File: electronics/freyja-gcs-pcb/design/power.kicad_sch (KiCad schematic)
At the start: 113 parts, among them J6 GT-USB-7010ASV, J7 A2543WR-4P-2, J8 XD-PH-10AW, J9 JS350-S02DCA-00, Q1 TM10N06SI, Q2 TM10N06SI, Q3 AO4459, Q4 L2N7002SLLT1G, Q5 L2N7002SLLT1G, Q6 TM10N06SI, Q7 TM10N06SI, Q8 TM10N06SI, SW3 K6-6136D-L1-04, U10 LM74700QDBVRQ1, U11 AMS1117-3.3, U12 RY3730, U3 FM7021DB, U4 CN3702, U5 HY2213-BB3A, U6 HY2213-BB3A, U7 IP2721, U8 SY8368AQQC, U9 LM74700QDBVRQ1

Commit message: power layout wip
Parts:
- C29: value 100n -> 22u; footprint Capacitor_SMD:C_0603_1608Metric -> EasyEDA:C1210; LCSC Part C2762593 -> C100086
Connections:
- net +5V: now also C29.1
- net VPWR: no longer C29.1
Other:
- moved on the sheet: C27, C28, C42, C44, D30, J9, L3, R37, TP7, U12

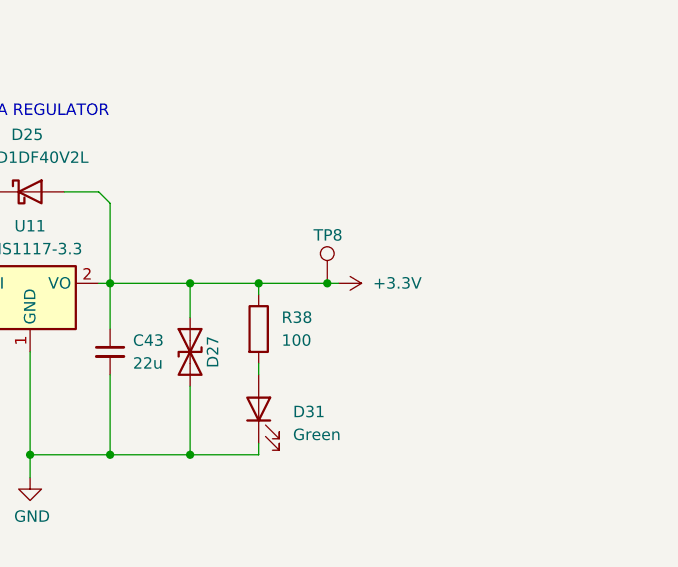
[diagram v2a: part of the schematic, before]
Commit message: locked position of components
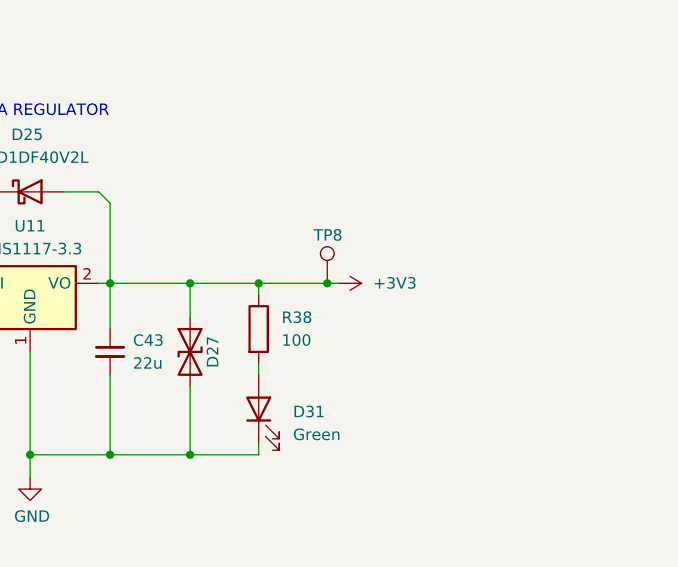
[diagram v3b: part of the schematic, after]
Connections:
- net +3.3V renamed +3V3
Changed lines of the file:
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@@
+	)
+	(symbol
+		(lib_id "power:+3V3")
+		(at 369.57 163.83 270)
+		(unit 1)
+		(exclude_from_sim no)
+		(in_bom yes)
+		(on_board yes)
+		(dnp no)
+		(fields_autoplaced yes)
+		(property "Reference" "#PWR0121"
+			(at 365.76 163.83 0)
+			(effects
+				(font
+					(size 1.27 1.27)
+				)
+				(hide yes)
+			)
+		)
+		(property "Value" "+3V3"
+			(at 373.38 163.8299 90)
+			(effects
+				(font
+					(size 1.27 1.27)
+				)
+				(justify left)
+			)
+		)
+		(property "Footprint" ""
+			(at 369.57 163.83 0)
+			(effects
+				(font
+					(size 1.27 1.27)
+				)
+				(hide yes)
+			)
+		)
+		(property "Datasheet" ""
+			(at 369.57 163.83 0)
+			(effects
+				(font
+					(size 1.27 1.27)
+				)
+				(hide yes)
+			)
+		)
+		(property "Description" "Power symbol creates a global label with name \"+3V3\""
+			(at 369.57 163.83 0)
+			(effects
+				(font
+					(size 1.27 1.27)
+				)
+				(hide yes)
+			)
+		)
+		(pin "1"
+		)
+		(instances
+			(project ""
+				(path "/c292fa04-82ad-49e9-a9d8-422554d1d11d/c65c6484-459d-48da-abd0-c2a58ebde1bb"
+					(reference "#PWR0121")
+					(unit 1)
+				)
+			)
+		)
 	)
 	(symbol
@@
 					(unit 1)
 				)
-			)
-		)
-	)
-	(symbol
-		(lib_id "power:+3.3V")
-		(at 369.57 163.83 270)
-		(unit 1)
-		(exclude_from_sim no)
-		(in_bom yes)
-		(on_board yes)
-		(dnp no)
-		(fields_autoplaced yes)
-		(property "Reference" "#PWR063"
-			(at 365.76 163.83 0)
-			(effects
-				(font
-					(size 1.27 1.27)
-				)
-				(hide yes)
-			)
-		)
-		(property "Value" "+3.3V"
-			(at 373.38 163.8299 90)
-			(effects
-				(font
-					(size 1.27 1.27)
-				)
-				(justify left)
-			)
-		)
-		(property "Footprint" ""
-			(at 369.57 163.83 0)
-			(effects
-				(font
-					(size 1.27 1.27)
-				)
-				(hide yes)
-			)
-		)
-		(property "Datasheet" ""
-			(at 369.57 163.83 0)
-			(effects
-				(font
-					(size 1.27 1.27)
-				)
-				(hide yes)
-			)
-		)
-		(property "Description" "Power symbol creates a global label with name \"+3.3V\""
-			(at 369.57 163.83 0)
-			(effects
-				(font
-					(size 1.27 1.27)
-				)
-				(hide yes)
-			)
-		)
-		(pin "1"
-		)
-		(instances
-			(project ""
-				(path "/c292fa04-82ad-49e9-a9d8-422554d1d11d/c65c6484-459d-48da-abd0-c2a58ebde1bb"
-					(reference "#PWR063")
-					(unit 1)
-				)

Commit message: mcu layout
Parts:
- added D59: PSBD1DF40V2L, EasyEDA:SOD-123FL_L2.8-W1.8-LS3.8-RD, symbol Device:D_Schottky
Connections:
- net +5V: now also D59.1 (K)
- net VBAT: now also U10.3 (EN)
- net VBUS: now also U9.3 (EN)
- net at C34.1, U9.1 (VCAP): no longer U9.3 (EN)
- net at C35.1, U10.1 (VCAP): no longer U10.3 (EN)
- new net VBUS_DEV: D59.2 (A)
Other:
- moved on the sheet: C30, C31, C32, C33, C34, C35, TP6

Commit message: usb pd layout
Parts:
- added D60: PESD2IVN24-TR, EasyEDA:TO-236AB_L2.9-W1.3-P0.95-LS2.3-BR, symbol EasyEDA:PESD2IVN24-TR
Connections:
- net GND: now also D60.3
- net at C23.1, J6.A4B9 (VBUS), J6.B4A9 (VBUS)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: now also D60.1, D60.2
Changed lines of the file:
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@@
 	)
 	(junction
+		(at 138.43 44.45)
+		(diameter 0)
+		(color 0 0 0 0)
+	)
+	(junction
 		(at 322.58 218.44)
 		(diameter 0)
@@
 	)
 	(junction
+		(at 148.59 44.45)
+		(diameter 0)
+		(color 0 0 0 0)
+	)
+	(junction
 		(at 262.89 207.01)
 		(diameter 0)
@@
 	(wire
 		(pts
+			(xy 148.59 44.45) (xy 148.59 49.53)
+		)
+		(stroke
+			(width 0)
+			(type default)
+		)
+	)
+	(wire
+		(pts
 			(xy 168.91 76.2) (xy 170.18 77.47)
 		)
@@
 	(wire
 		(pts
-			(xy 93.98 44.45) (xy 137.16 44.45)
+			(xy 93.98 44.45) (xy 138.43 44.45)
 		)
 		(stroke
@@
 	(wire
 		(pts
-			(xy 138.43 45.72) (xy 138.43 63.5)
+			(xy 138.43 44.45) (xy 138.43 63.5)
 		)
 		(stroke
@@
 	(wire
 		(pts
+			(xy 173.99 46.99) (xy 175.26 46.99)
+		)
+		(stroke
+			(width 0)
+			(type default)
+		)
+	)
+	(wire
+		(pts
 			(xy 39.37 176.53) (xy 48.26 176.53)
 		)
@@
 	(wire
 		(pts
-			(xy 137.16 44.45) (xy 138.43 45.72)
-		)
-		(stroke
-			(width 0)
-			(type default)
-		)
-	)
-	(wire
-		(pts
 			(xy 85.09 167.64) (xy 85.09 168.91)
 		)
@@
 	(wire
 		(pts
+			(xy 175.26 46.99) (xy 175.26 48.26)
+		)
+		(stroke
+			(width 0)
+			(type default)
+		)
+	)
+	(wire
+		(pts
 			(xy 96.52 154.94) (xy 96.52 168.91)
 		)
@@
 	(wire
 		(pts
+			(xy 138.43 44.45) (xy 148.59 44.45)
+		)
+		(stroke
+			(width 0)
+			(type default)
+		)
+	)
+	(wire
+		(pts
 			(xy 246.38 101.6) (xy 246.38 104.14)
 		)
@@
 	)
 	(symbol
+		(lib_id "EasyEDA:PESD2IVN24-TR")
+		(at 161.29 46.99 0)
+		(mirror x)
+		(unit 1)
+		(exclude_from_sim no)
+		(in_bom yes)
+		(on_board yes)
+		(dnp no)
+		(property "Reference" "D60"
+			(at 160.0199 53.34 90)
+			(effects
+				(font
+					(size 1.27 1.27)
+				)
+				(justify left)
+			)
+		)
+		(property "Value" "PESD2IVN24-TR"
+			(at 162.5599 53.34 90)
+			(effects
+				(font
+					(size 1.27 1.27)
+				)
+				(justify left)
+			)
+		)
+		(property "Footprint" "EasyEDA:TO-236AB_L2.9-W1.3-P0.95-LS2.3-BR"
+			(at 161.29 36.83 0)
+			(effects
+				(font
+					(size 1.27 1.27)
+				)
+				(hide yes)
+			)
+		)
+		(property "Datasheet" "https://lcsc.com/product-detail/Zener-Diodes_Nexperia-PESD2IVN24-TR_C406047.html"
+			(at 161.29 34.29 0)
+			(effects
+				(font
+					(size 1.27 1.27)
+				)
+				(hide yes)
+			)
+		)
+		(property "Description" ""
+			(at 161.29 46.99 0)
+			(effects
+				(font
+					(size 1.27 1.27)
+				)
+				(hide yes)
+			)
+		)
+		(property "LCSC Part" "C406047"
+			(at 161.29 31.75 0)
+			(effects
+				(font
+					(size 1.27 1.27)
+				)
+				(hide yes)
+			)
+		)
+		(pin "2"
+		)
+		(pin "3"
+		)
+		(pin "1"
+		)
+		(instances
+			(project "freyja-gcs-pcb"
+				(path "/c292fa04-82ad-49e9-a9d8-422554d1d11d/c65c6484-459d-48da-abd0-c2a58ebde1bb"
+					(reference "D60")
+					(unit 1)
+				)
+			)
+		)
+	)
+	(symbol
 		(lib_id "Device:R")
 		(at 274.32 201.93 270)
@@
 					(unit 1)
 				)
+			)
+		)
+	)
+	(symbol
+		(lib_id "power:GND")
+		(at 175.26 48.26 0)
+		(mirror y)
+		(unit 1)
+		(exclude_from_sim no)
+		(in_bom yes)
+		(on_board yes)
+		(dnp no)
+		(property "Reference" "#PWR05"
+			(at 175.26 54.61 0)
+			(effects
+				(font
+					(size 1.27 1.27)
+				)
+				(hide yes)
+			)
+		)
+		(property "Value" "GND"
+			(at 173.482 52.578 0)
+			(effects
+				(font
+					(size 1.27 1.27)
+				)
+				(justify right)
+			)
+		)
+		(property "Footprint" ""
+			(at 175.26 48.26 0)
+			(effects
+				(font
+					(size 1.27 1.27)
+				)
+				(hide yes)
+			)
+		)
+		(property "Datasheet" ""
+			(at 175.26 48.26 0)
+			(effects
+				(font
+					(size 1.27 1.27)
+				)
+				(hide yes)
+			)
+		)
+		(property "Description" "Power symbol creates a global label with name \"GND\" , ground"
+			(at 175.26 48.26 0)
+			(effects
+				(font
+					(size 1.27 1.27)
+				)
+				(hide yes)
+			)
+		)
+		(pin "1"
+		)
+		(instances
+			(project "freyja-gcs-pcb"
+				(path "/c292fa04-82ad-49e9-a9d8-422554d1d11d/c65c6484-459d-48da-abd0-c2a58ebde1bb"
+					(reference "#PWR05")
+					(unit 1)
+				)

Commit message: charging circuit layout wip
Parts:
- added C49: 22u, EasyEDA:C2220, symbol Device:C_Small
- added TP10: TestPoint, TestPoint:TestPoint_Pad_D3.0mm, symbol Connector:TestPoint
- C20: value 100n -> 470n; LCSC Part C2762593 -> C513577
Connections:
- net BAT-: no longer R11.2
- net GND: now also C49.2
- net VBAT: now also C49.1
- net at BT4.1 (-), BT5.2 (+), C21.2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: now also BT2.1 (-), BT3.2 (+), TP10.1
- net at U3.3 (CS): now also R11.2
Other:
- moved on the sheet: Q1, Q2, R11

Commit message: btn routing wip
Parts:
- D13: footprint EasyEDA:LED0603-RD_GREEN -> EasyEDA:LED-TH_BD5.9-P2.54-RD_GREEN; LCSC Part C965804 -> C2895548
- D14: value Amber -> Yellow; footprint EasyEDA:LED0603-R-RD_AMBER -> EasyEDA:LED-TH_BD5.9-P2.54-RD_GREEN; LCSC Part C510024 -> C2895494
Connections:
- net at U4.4 (~{CHRG}): now also D14.1 (K); no longer D14.2 (K)
- net at R15.2: now also D14.2 (A); no longer D14.1 (A)
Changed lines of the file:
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@@
 	)
 	(symbol
-		(lib_name "LED_1")
-		(lib_id "Device:LED")
-		(at 35.56 143.51 90)
-		(unit 1)
-		(exclude_from_sim no)
-		(in_bom yes)
-		(on_board yes)
-		(dnp no)
-		(fields_autoplaced yes)
-		(property "Reference" "D14"
-			(at 39.37 143.8274 90)
-			(effects
-				(font
-					(size 1.27 1.27)
-				)
-				(justify right)
-			)
-		)
-		(property "Value" "Amber"
-			(at 39.37 146.3674 90)
-			(effects
-				(font
-					(size 1.27 1.27)
-				)
-				(justify right)
-			)
-		)
-		(property "Footprint" "EasyEDA:LED0603-R-RD_AMBER"
-			(at 35.56 143.51 0)
-			(effects
-				(font
-					(size 1.27 1.27)
-				)
-				(hide yes)
-			)
-		)
-		(property "Datasheet" "~"
-			(at 35.56 143.51 0)
-			(effects
-				(font
-					(size 1.27 1.27)
-				)
-				(hide yes)
-			)
-		)
-		(property "Description" "SML-D12D8WT86 Light emitting diode"
-			(at 35.56 143.51 0)
-			(effects
-				(font
-					(size 1.27 1.27)
-				)
-				(hide yes)
-			)
-		)
-		(property "LCSC Part" "C510024"
-			(at 45.72 143.51 0)
-			(effects
-				(font
-					(size 1.27 1.27)
-				)
-				(hide yes)
-			)
-		)
-		(property "Sim.Pins" "1=A 2=K"
-			(at 35.56 143.51 0)
-			(effects
-				(font
-					(size 1.27 1.27)
-				)
-				(hide yes)
-			)
-		)
-		(pin "2"
-		)
-		(pin "1"
-		)
-		(instances
-			(project "freyja-gcs-pcb"
-				(path "/c292fa04-82ad-49e9-a9d8-422554d1d11d/c65c6484-459d-48da-abd0-c2a58ebde1bb"
-					(reference "D14")
-					(unit 1)
-				)
-			)
-		)
-	)
-	(symbol
 		(lib_id "EasyEDA:AO4459")
 		(at 92.71 132.08 270)
@@
 	)
 	(symbol
+		(lib_id "Device:LED")
+		(at 30.48 143.51 270)
+		(mirror x)
+		(unit 1)
+		(exclude_from_sim no)
+		(in_bom yes)
+		(on_board yes)
+		(dnp no)
+		(property "Reference" "D13"
+			(at 26.67 143.8274 90)
+			(effects
+				(font
+					(size 1.27 1.27)
+				)
+				(justify right)
+			)
+		)
+		(property "Value" "Green"
+			(at 26.67 146.3674 90)
+			(effects
+				(font
+					(size 1.27 1.27)
+				)
+				(justify right)
+			)
+		)
+		(property "Footprint" "EasyEDA:LED-TH_BD5.9-P2.54-RD_GREEN"
+			(at 30.48 143.51 0)
+			(effects
+				(font
+					(size 1.27 1.27)
+				)
+				(hide yes)
+			)
+		)
+		(property "Datasheet" "~"
+			(at 30.48 143.51 0)
+			(effects
+				(font
+					(size 1.27 1.27)
+				)
+				(hide yes)
+			)
+		)
+		(property "Description" "XL-502UGD Light emitting diode"
+			(at 30.48 143.51 0)
+			(effects
+				(font
+					(size 1.27 1.27)
+				)
+				(hide yes)
+			)
+		)
+		(property "LCSC Part" "C2895548"
+			(at 20.32 143.51 0)
+			(effects
+				(font
+					(size 1.27 1.27)
+				)
+				(hide yes)
+			)
+		)
+		(property "Sim.Pins" "1=K 2=A"
+			(at 30.48 143.51 0)
+			(effects
+				(font
+					(size 1.27 1.27)
+				)
+				(hide yes)
+			)
+		)
+		(pin "2"
+		)
+		(pin "1"
+		)
+		(instances
+			(project "freyja-gcs-pcb"
+				(path "/c292fa04-82ad-49e9-a9d8-422554d1d11d/c65c6484-459d-48da-abd0-c2a58ebde1bb"
+					(reference "D13")
+					(unit 1)
+				)
+			)
+		)
+	)
+	(symbol
 		(lib_id "power:GND")
 		(at 346.71 125.73 0)
@@
 	)
 	(symbol
+		(lib_id "Device:LED")
+		(at 35.56 143.51 90)
+		(unit 1)
+		(exclude_from_sim no)
+		(in_bom yes)
+		(on_board yes)
+		(dnp no)
+		(property "Reference" "D14"
+			(at 39.37 143.8274 90)
+			(effects
+				(font
+					(size 1.27 1.27)
+				)
+				(justify right)
+			)
+		)
+		(property "Value" "Yellow"
+			(at 39.37 146.3674 90)
+			(effects
+				(font
+					(size 1.27 1.27)
+				)
+				(justify right)
+			)
+		)
+		(property "Footprint" "EasyEDA:LED-TH_BD5.9-P2.54-RD_GREEN"
+			(at 35.56 143.51 0)
+			(effects
+				(font
+					(size 1.27 1.27)
+				)
+				(hide yes)
+			)
+		)
+		(property "Datasheet" "~"
+			(at 35.56 143.51 0)
+			(effects
+				(font
+					(size 1.27 1.27)
+				)
+				(hide yes)
+			)
+		)
+		(property "Description" "XL-502UYD Light emitting diode"
+			(at 35.56 143.51 0)
+			(effects
+				(font
+					(size 1.27 1.27)
+				)
+				(hide yes)
+			)
+		)
+		(property "LCSC Part" "C2895494"
+			(at 45.72 143.51 0)
+			(effects
+				(font
+					(size 1.27 1.27)
+				)
+				(hide yes)
+			)
+		)
+		(property "Sim.Pins" "1=K 2=A"
+			(at 35.56 143.51 0)
+			(effects
+				(font
+					(size 1.27 1.27)
+				)
+				(hide yes)
+			)
+		)
+		(pin "2"
+		)
+		(pin "1"
+		)
+		(instances
+			(project "freyja-gcs-pcb"
+				(path "/c292fa04-82ad-49e9-a9d8-422554d1d11d/c65c6484-459d-48da-abd0-c2a58ebde1bb"
+					(reference "D14")
+					(unit 1)
+				)
+			)
+		)
+	)
+	(symbol
 		(lib_id "Connector:TestPoint")
 		(at 173.99 246.38 270)
@@
 					(unit 1)
 				)
-			)
-		)
-	)
-	(symbol
-		(lib_id "Device:LED")
-		(at 30.48 143.51 270)
-		(mirror x)
-		(unit 1)
-		(exclude_from_sim no)
-		(in_bom yes)
-		(on_board yes)
-		(dnp no)
-		(property "Reference" "D13"
-			(at 26.67 143.8274 90)
-			(effects
-				(font
-					(size 1.27 1.27)
-				)
-				(justify right)
-			)
-		)
-		(property "Value" "Green"
-			(at 26.67 146.3674 90)
-			(effects
-				(font
-					(size 1.27 1.27)
-				)
-				(justify right)
-			)
-		)
-		(property "Footprint" "EasyEDA:LED0603-RD_GREEN"
-			(at 30.48 143.51 0)
-			(effects
-				(font
-					(size 1.27 1.27)
-				)
-				(hide yes)
-			)
-		)
-		(property "Datasheet" "~"
-			(at 30.48 143.51 0)
-			(effects
-				(font
-					(size 1.27 1.27)
-				)
-				(hide yes)
-			)
-		)
-		(property "Description" "XL-1608UGC-04 Light emitting diode"
-			(at 30.48 143.51 0)
-			(effects
-				(font
-					(size 1.27 1.27)
-				)
-				(hide yes)
-			)
-		)
-		(property "LCSC Part" "C965804"
-			(at 20.32 143.51 0)
-			(effects
-				(font
-					(size 1.27 1.27)
-				)
-				(hide yes)
-			)
-		)
-		(property "Sim.Pins" "1=K 2=A"
-			(at 30.48 143.51 0)
-			(effects
-				(font
-					(size 1.27 1.27)
-				)
-				(hide yes)
-			)
-		)
-		(pin "2"
-		)
-		(pin "1"
-		)
-		(instances
-			(project ""
-				(path "/c292fa04-82ad-49e9-a9d8-422554d1d11d/c65c6484-459d-48da-abd0-c2a58ebde1bb"
-					(reference "D13")
-					(unit 1)
-				)

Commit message: all routed, fine tuning left
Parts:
- added C50, C51, C52, C53, C54: 100n, Capacitor_SMD:C_0603_1608Metric, symbol Device:C_Small
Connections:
- net +5V: now also C50.2, C51.2, C52.2, C53.2
- net GND: now also C50.1, C51.1, C52.1, C53.1, C54.1
- net VBUS: now also C54.2
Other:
- note added: "CAPACITORS ON TRACE STUBS TO REDUCE EMI RADIATION"
